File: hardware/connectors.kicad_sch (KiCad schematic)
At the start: 18 parts, among them J2 Screw_Terminal_01x04

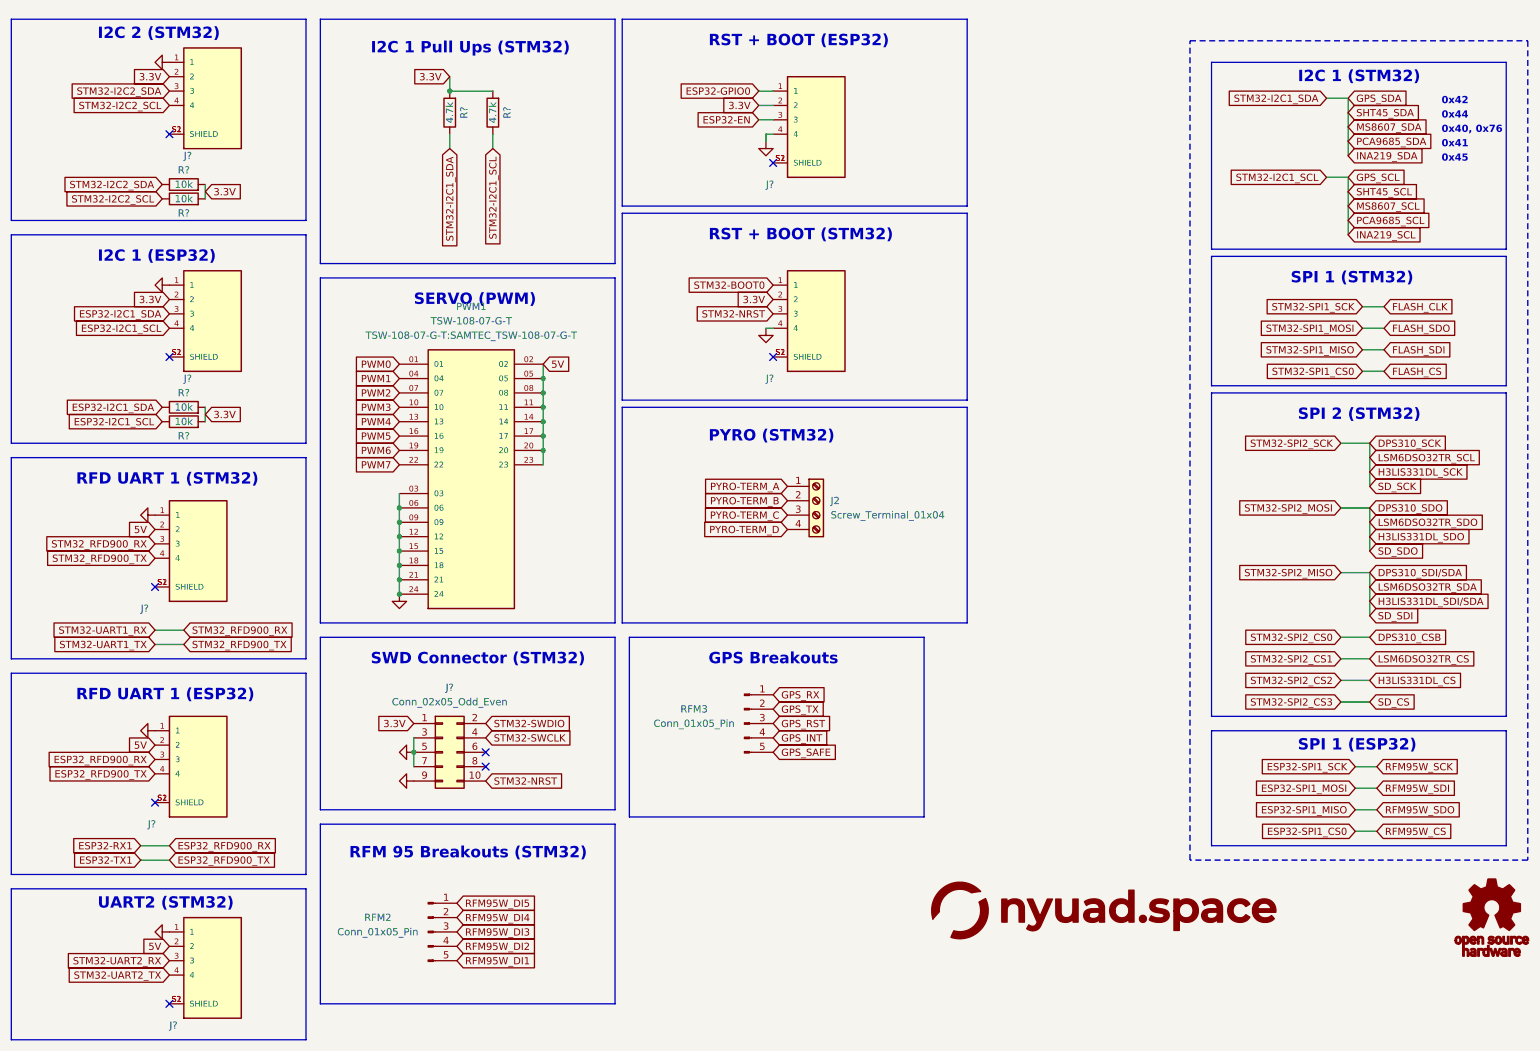
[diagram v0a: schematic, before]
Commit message: added BNO086
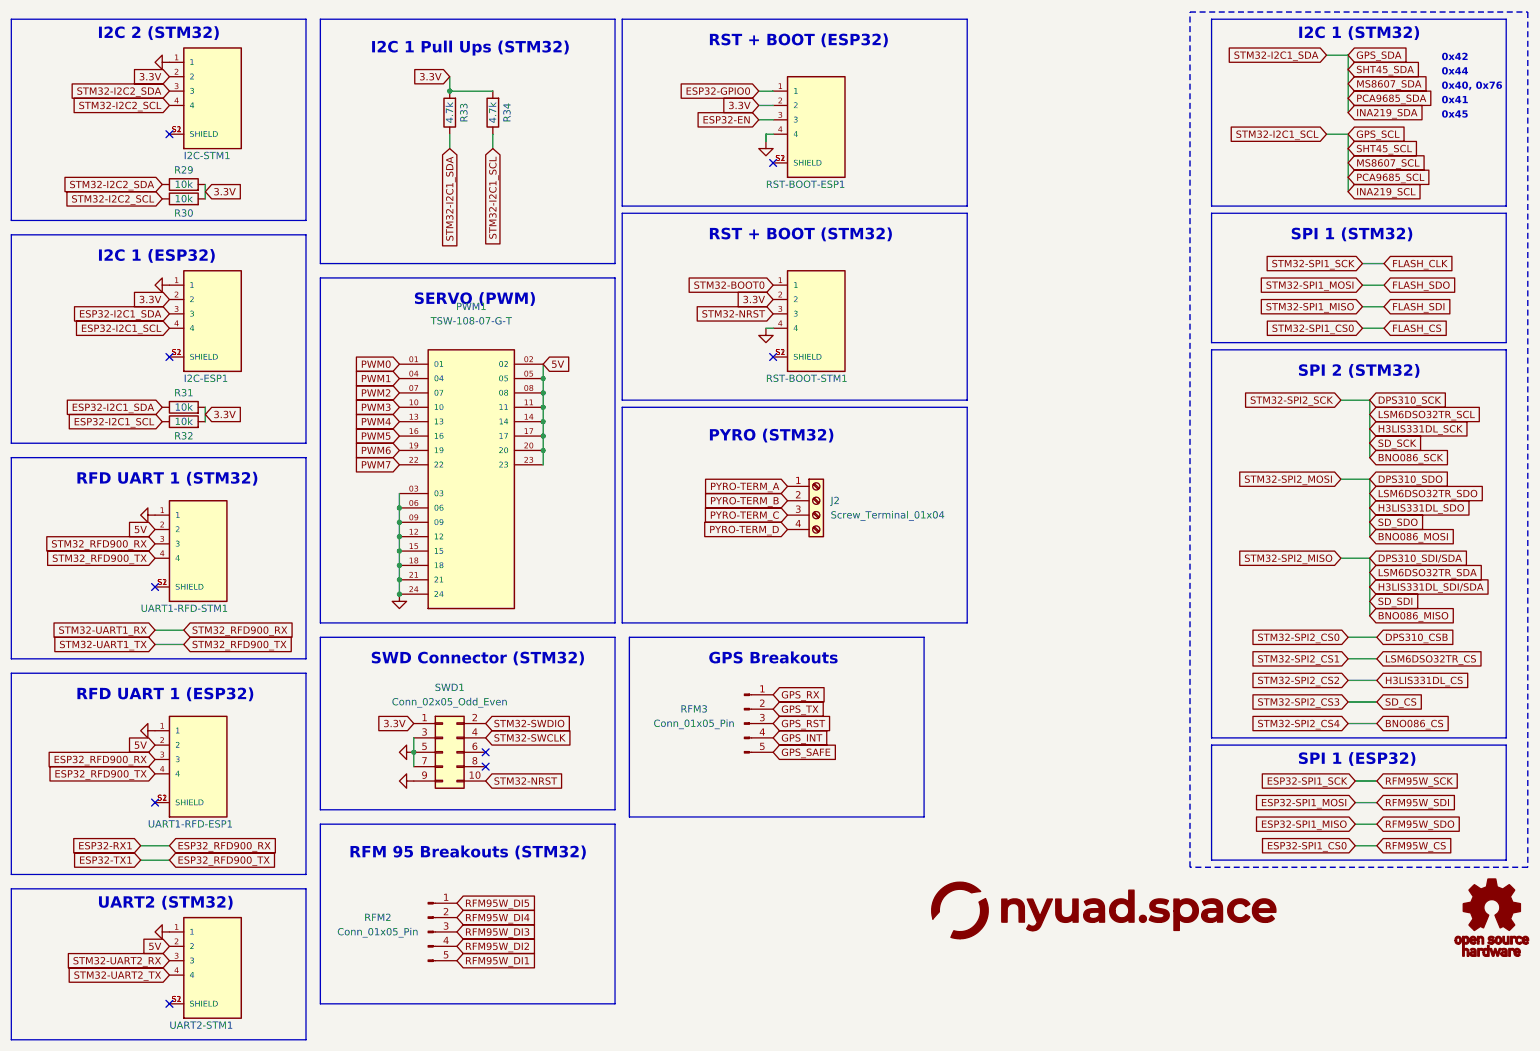
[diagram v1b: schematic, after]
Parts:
- I2C-ESP1, I2C-STM1, RST-BOOT-ESP1, RST-BOOT-STM1, UART1-RFD-ESP1, UART1-RFD-STM1, UART2-STM1: renamed from J?; footprint JST_SM04B-SRSS-TB(LF)(SN) -> (none)
- J2: footprint TerminalBlock_TE-Connectivity:TerminalBlock_TE_282834-4_1x04_P2.54mm_Horizontal -> (none)
- PWM1: footprint TSW-108-07-G-T:SAMTEC_TSW-108-07-G-T -> (none)
- R29, R30, R31, R32, R33, R34: renamed from R?; footprint Resistor_SMD:R_0402_1005Metric -> (none)
- RFM2, RFM3: footprint Connector_PinHeader_1.27mm:PinHeader_1x05_P1.27mm_Vertical -> (none)
- SWD1: renamed from J?; footprint Connector_PinHeader_1.27mm:PinHeader_2x05_P1.27mm_Vertical_SMD -> (none)

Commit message: rev2 component placement
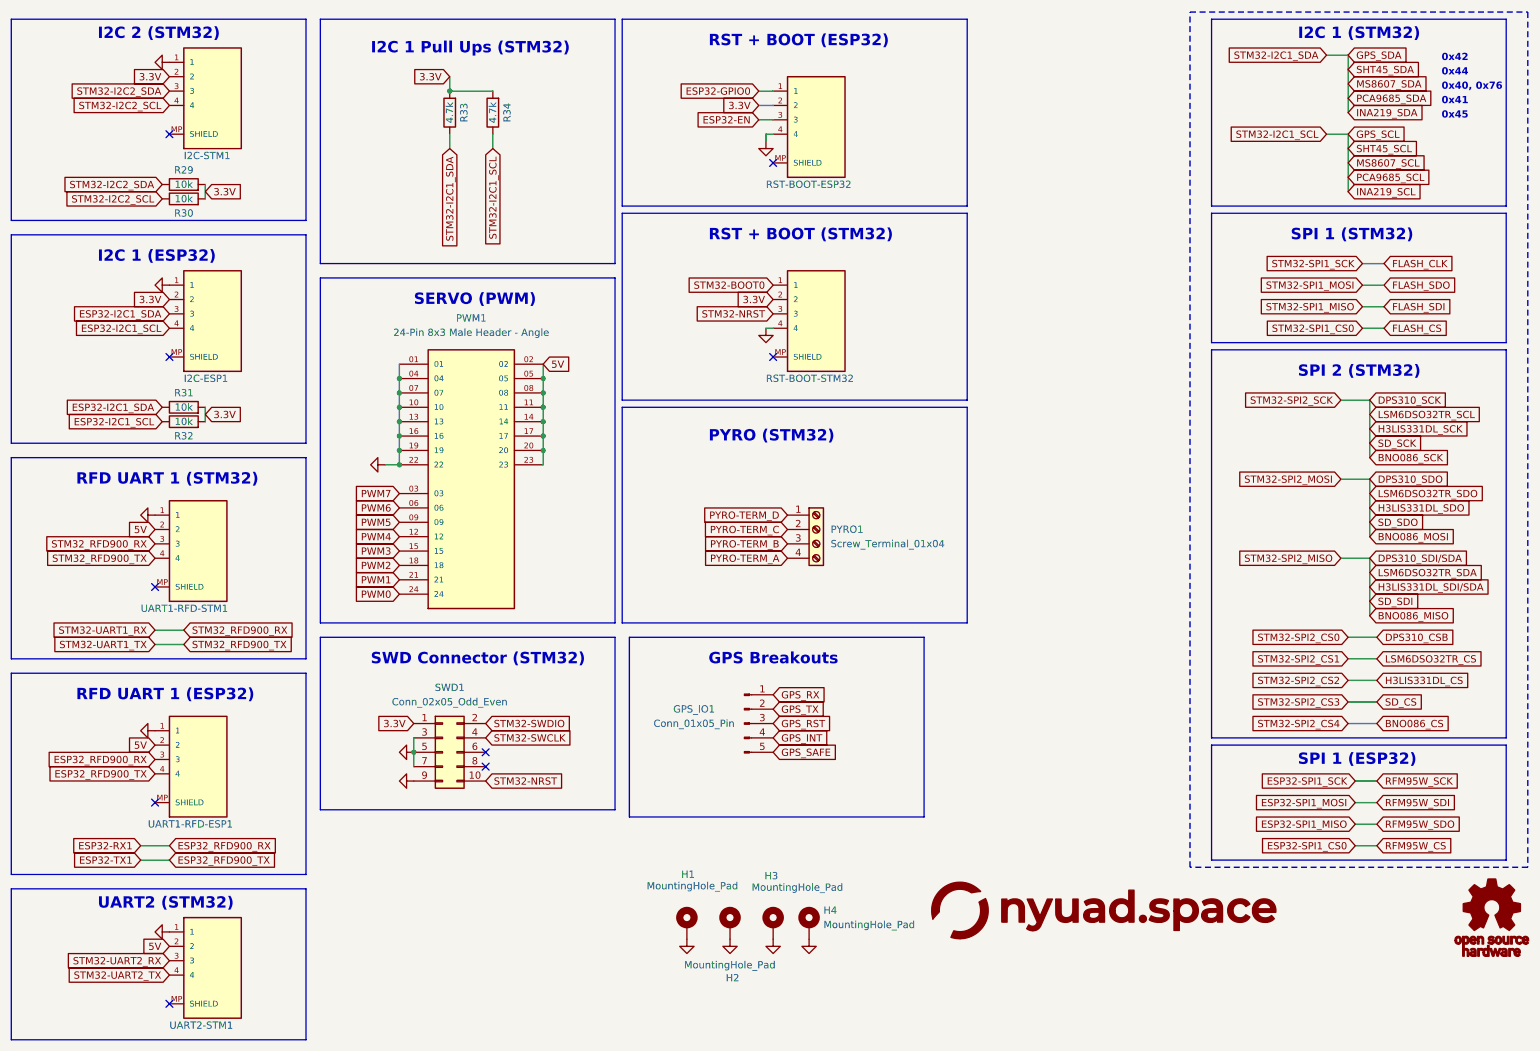
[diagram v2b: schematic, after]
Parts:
- removed J2: Screw_Terminal_01x04, symbol Connector:Screw_Terminal_01x04
- removed RFM2: Conn_01x05_Pin, symbol Connector:Conn_01x05_Pin
- added H1, H2, H3, H4: MountingHole_Pad, MountingHole:MountingHole_3.2mm_M3_Pad_Via, symbol Mechanical:MountingHole_Pad
- added PYRO1: Screw_Terminal_01x04, TerminalBlock:TerminalBlock_Xinya_XY308-2.54-4P_1x04_P2.54mm_Horizontal, symbol Connector:Screw_Terminal_01x04
- GPS_IO1: renamed from RFM3; footprint (none) -> Connector_PinHeader_1.27mm:PinHeader_1x05_P1.27mm_Vertical
- I2C-ESP1, I2C-STM1, UART1-RFD-ESP1, UART1-RFD-STM1, UART2-STM1: footprint (none) -> Connector_JST:JST_SH_SM04B-SRSS-TB_1x04-1MP_P1.00mm_Horizontal
- PWM1: value TSW-108-07-G-T -> 24-Pin 8x3 Male Header - Angle; footprint (none) -> TSW-108-08-T-T-RA:SAMTEC_TSW-108-08-T-T-RA
- R29, R30, R31, R32, R33, R34: footprint (none) -> Resistor_SMD:R_0402_1005Metric
- RST-BOOT-ESP32: renamed from RST-BOOT-ESP1; footprint (none) -> Connector_JST:JST_SH_SM04B-SRSS-TB_1x04-1MP_P1.00mm_Horizontal
- RST-BOOT-STM32: renamed from RST-BOOT-STM1; footprint (none) -> Connector_JST:JST_SH_SM04B-SRSS-TB_1x04-1MP_P1.00mm_Horizontal
- SWD1: footprint (none) -> Connector_PinHeader_1.27mm:PinHeader_2x05_P1.27mm_Vertical_SMD
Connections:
- net GND: now also PWM1.01, PWM1.04, PWM1.07, PWM1.10, PWM1.13, PWM1.16, PWM1.19, PWM1.22, H1.1, H2.1, H3.1, H4.1; no longer PWM1.03, PWM1.06, PWM1.09, PWM1.12, PWM1.15, PWM1.18, PWM1.21, PWM1.24
- net PWM0: now also PWM1.24; no longer PWM1.01
- net PWM1: now also PWM1.21; no longer PWM1.04
- net PWM2: now also PWM1.18; no longer PWM1.07
- net PWM3: now also PWM1.15; no longer PWM1.10
- net PWM4: now also PWM1.12; no longer PWM1.13
- net PWM5: now also PWM1.09; no longer PWM1.16
- net PWM6: now also PWM1.06; no longer PWM1.19
- net PWM7: now also PWM1.03; no longer PWM1.22
- net PYRO-TERM_A: now also PYRO1.4 (Pin_4)
- net PYRO-TERM_B: now also PYRO1.3 (Pin_3)
- net PYRO-TERM_C: now also PYRO1.2 (Pin_2)
- net PYRO-TERM_D: now also PYRO1.1 (Pin_1)
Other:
- note removed: "RFM 95 Breakouts (STM32)"
